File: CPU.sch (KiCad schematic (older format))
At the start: 1 part, among them P55 9S12XDP512

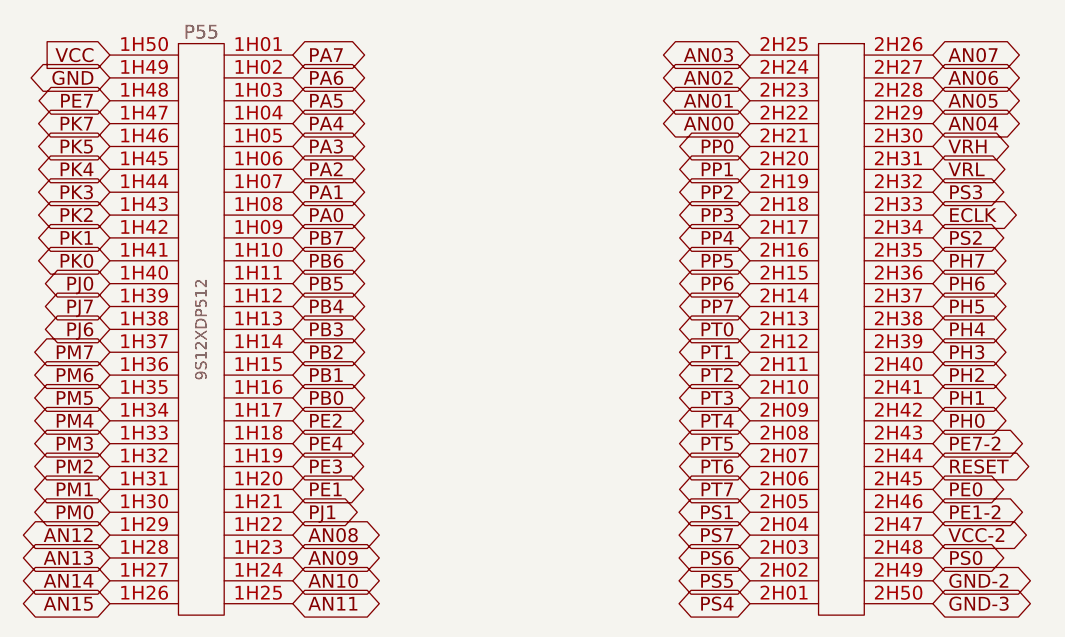
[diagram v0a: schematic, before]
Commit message: DFH mans up a bit. Perhaps usable for something at this point, like making trips to the local store ;)
I connected TA pins to sub circuits, fixed a number if items discussed in the DIYEFI forums. This is it's 21st version, so it was time for it to man up a bit, and become something potentially useful.

Signed-off-by: Jared Harvey <TortiseGIT@jaredharvey.com>
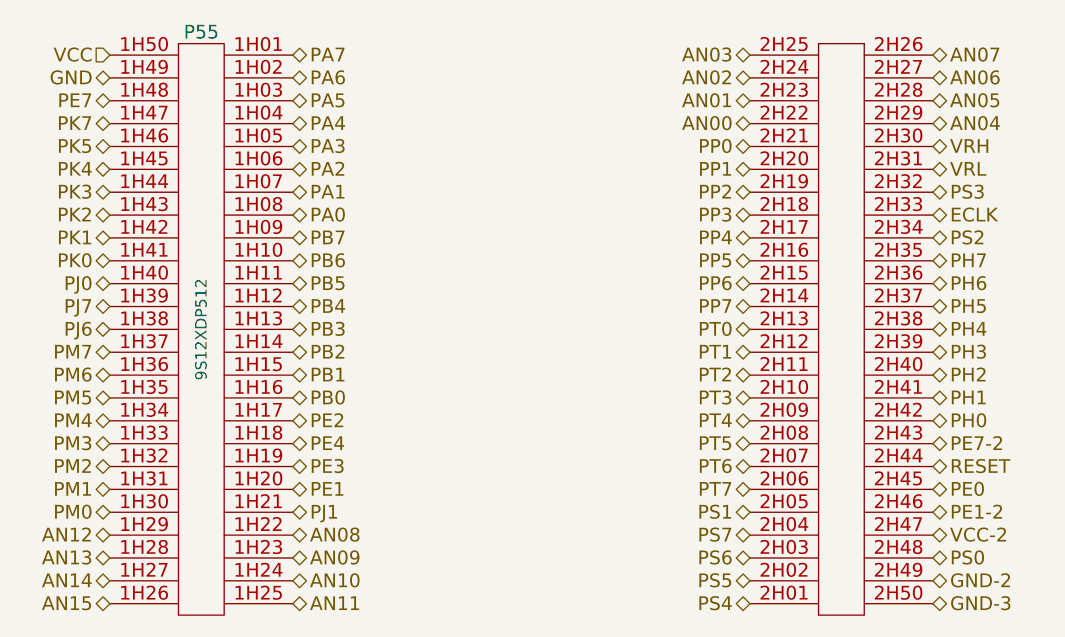
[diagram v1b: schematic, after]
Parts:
- P55: Field10 (none) -> x; Field11 (none) -> other,more,stuff; Field4 (none) -> vendor1, thru w hem; Field5 (none) -> vendor1, smd w hem; Field6 (none) -> vendor2, thru w hem; Field7 (none) -> vendor2, smd w hem; Field8 (none) -> x,x; Field9 (none) -> x,x
